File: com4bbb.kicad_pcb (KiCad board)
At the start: 2 copper layers, 54.6 x 86.4 mm, 50 parts, among them J101 PWR, J102 RS485, P8 BeagleBone_Black_Header, P9 BeagleBone_Black_Header, SW101 Reset, SW102 PWR, U101 WPMDH1100xx1S, U102 AT24C512C-SSHD-T, U103 SP3485EN, U104 ESP32-WROOM-32U

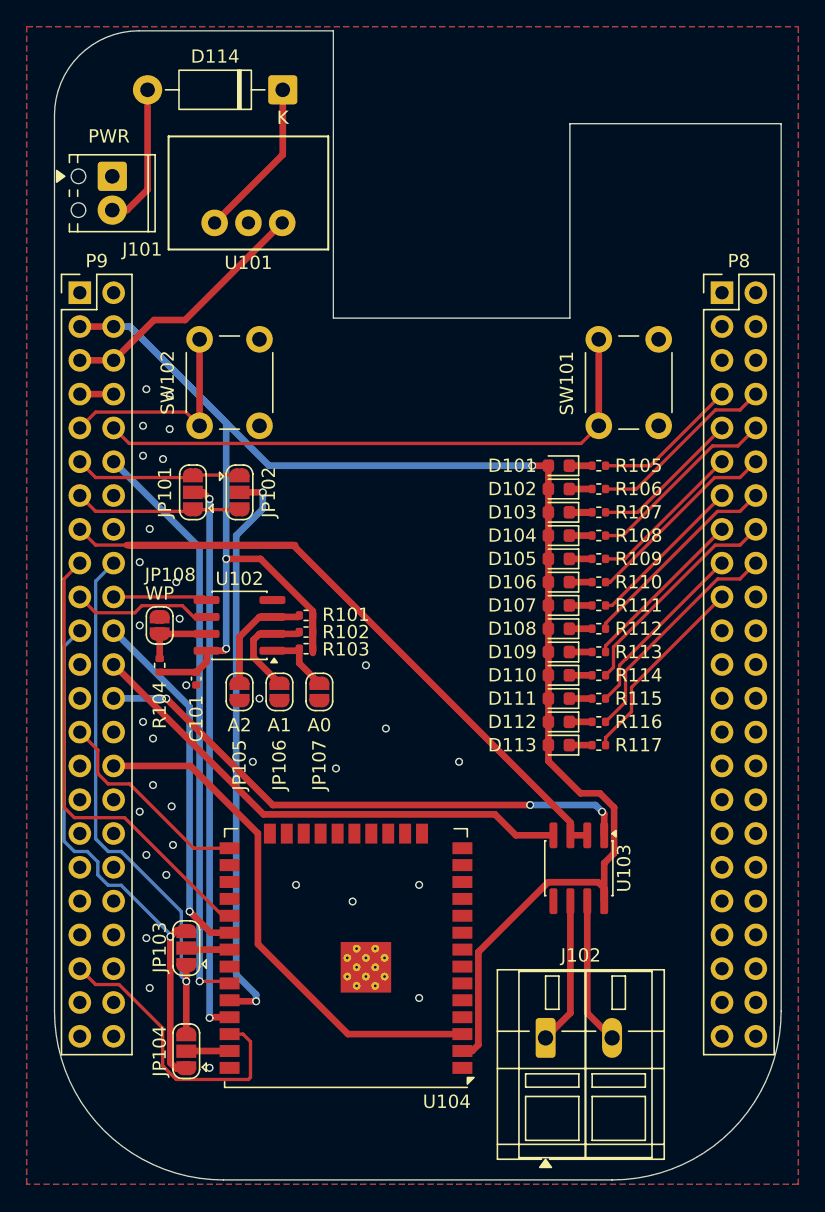
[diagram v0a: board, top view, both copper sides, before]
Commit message: Update to ESP32-S3-WROOM-1U
Signed-off-by: Benedikt Spranger <bene@eurovibes.org>
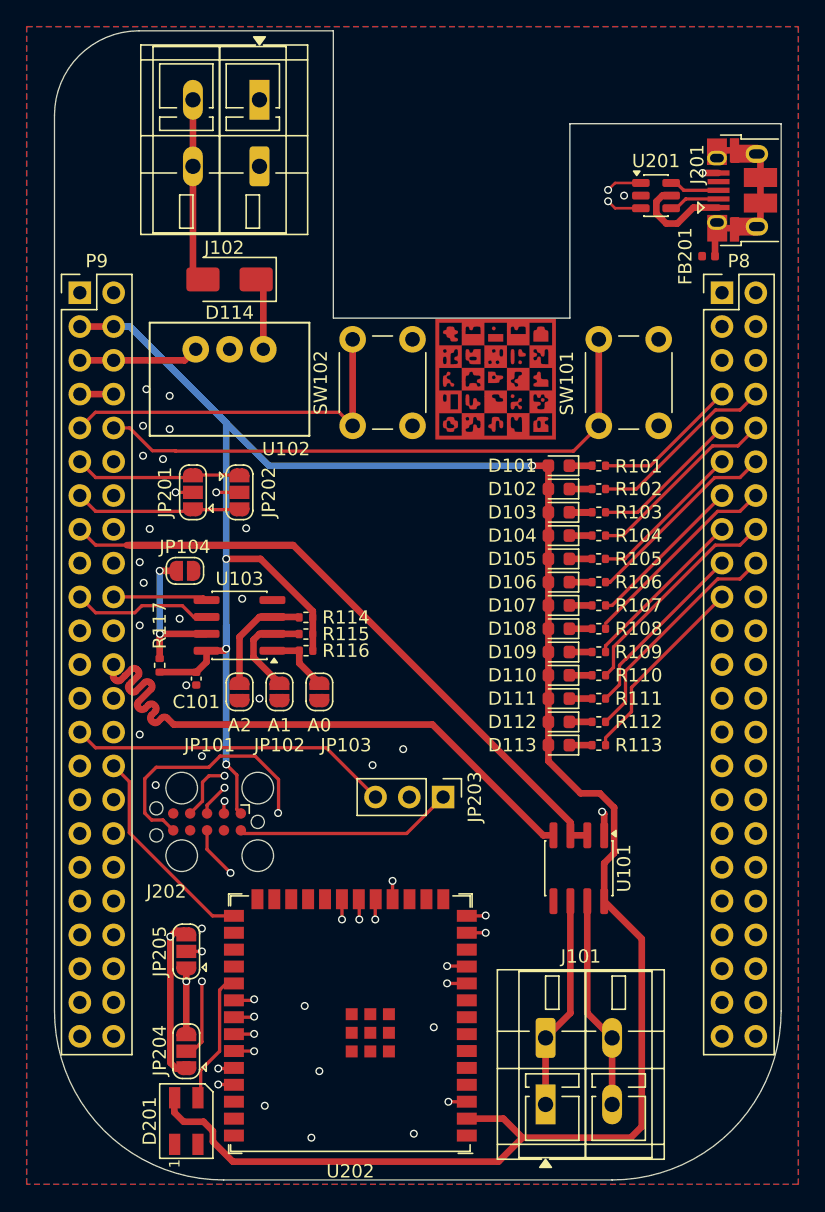
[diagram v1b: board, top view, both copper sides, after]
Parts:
- removed JP108: WP, Jumper:SolderJumper-2_P1.3mm_Open_RoundedPad1.0x1.5mm
- removed U104: ESP32-WROOM-32U, RF_Module:ESP32-WROOM-32U
- added D201: SK6812MINI, LED_SMD:LED_SK6812MINI_PLCC4_3.5x3.5mm_P1.75mm, F.Cu at (124.4, 124.6)
- added FB201: FerriteBead_Small, Inductor_SMD:L_0402_1005Metric, F.Cu at (163.6, 59.6)
- added G***: LOGO, eurovibes:LOGO, F.Cu at (147.6, 68.9)
- added J201: USB_B_Micro, Connector_USB:USB_Micro-B_Amphenol_10103594-0001LF_Horizontal, F.Cu at (166.1, 54.7)
- added J202: JTAG, Connector:Tag-Connect_TC2050-IDC-FP_2x05_P1.27mm_Vertical, F.Cu at (125.9, 102.1)
- added JP104: WP, Jumper:SolderJumper-2_P1.3mm_Open_RoundedPad1.0x1.5mm, F.Cu at (124.3, 83.3)
- added JP203: JTAG, Connector_PinHeader_2.54mm:PinHeader_1x03_P2.54mm_Vertical, F.Cu at (143.7, 100.3)
- added U201: USBLC6-2SC6, Package_TO_SOT_SMD:SOT-23-6, F.Cu at (159.7, 55.1)
- added U202: ESP32-S3-WROOM-1, PCM_Espressif:ESP32-S3-WROOM-1U, F.Cu at (136.7, 117.5)
- D114: value 1N4004 -> MRA4004T3G; footprint Diode_THT:D_DO-41_SOD81_P10.16mm_Horizontal -> Diode_SMD:D_SMA
- J101: renamed from J102; footprint TerminalBlock_WAGO:TerminalBlock_WAGO_236-102_1x02_P5.00mm_45Degree -> TerminalBlock_WAGO:TerminalBlock_WAGO_236-402_1x02_P5.00mm_45Degree
- J102: renamed from J101; footprint TerminalBlock_Phoenix:TerminalBlock_Phoenix_MPT-0,5-2-2.54_1x02_P2.54mm_Horizontal -> TerminalBlock_WAGO:TerminalBlock_WAGO_236-402_1x02_P5.00mm_45Degree
- moved R104 34.4 mm to (155.4, 80.6), turned to 0 degrees
- moved R117 33.5 mm to (122.4, 90.4), turned to 90 degrees
- moved R101 24.7 mm to (155.4, 75.4), turned to 0 degrees
- moved R102 24.5 mm to (155.4, 77.1), turned to 0 degrees
- moved R103 24.3 mm to (155.4, 78.9), turned to 0 degrees
- moved R116 22.6 mm to (133.4, 89.3), turned to 180 degrees
- moved R115 22.5 mm to (133.4, 88.0), turned to 180 degrees
- moved R114 22.4 mm to (133.4, 86.8), turned to 180 degrees
- moved D114 14.8 mm to (127.6, 61.4)
- moved SW102 11.5 mm to (136.9, 72.4)
- moved J102 11.1 mm to (129.9, 52.9), turned to 180 degrees
- moved U102 9.61 mm to (127.6, 66.6), turned to 180 degrees
- moved JP204 7.75 mm to (124.4, 119.4)
- moved JP205 7.50 mm to (124.4, 111.9)
- moved R105 7.00 mm to (155.4, 82.4)
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- renumbered JP105 to JP101, JP106 to JP102, JP107 to JP103, JP101 to JP201, JP102 to JP202, JP103 to JP204, JP104 to JP205, U103 to U101, U101 to U102, U102 to U103
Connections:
- JP101 pad 1: Net-(JP105-A) -> Net-(JP101-A)
- JP102 pad 1: Net-(JP106-A) -> Net-(JP102-A)
- JP103 pad 1: Net-(JP107-A) -> Net-(JP103-A)
- JP204 pad 1: /SPI0_D1 -> /SPI0_D0
- JP204 pad 3: /SPI0_D0 -> /SPI0_D1
- JP205 pad 1: /SPI0_D0 -> /SPI0_D1
- JP205 pad 3: /SPI0_D1 -> /SPI0_D0
- R101 pad 1: +3V3 -> Net-(D101-K)
- R101 pad 2: Net-(JP105-A) -> /LED0
- R102 pad 1: +3V3 -> Net-(D102-K)
- R102 pad 2: Net-(JP106-A) -> /LED1
- R103 pad 1: +3V3 -> Net-(D103-K)
- R103 pad 2: Net-(JP107-A) -> /LED2
- R104 pad 1: +3V3 -> Net-(D104-K)
- R104 pad 2: Net-(JP108-A) -> /LED3
- R105 pad 1: Net-(D101-K) -> Net-(D105-K)
- R105 pad 2: /LED0 -> /LED4
- R106 pad 1: Net-(D102-K) -> Net-(D106-K)
- R106 pad 2: /LED1 -> /LED5
- R107 pad 1: Net-(D103-K) -> Net-(D107-K)
- R107 pad 2: /LED2 -> /LED6
- R108 pad 1: Net-(D104-K) -> Net-(D108-K)
- R108 pad 2: /LED3 -> /LED7
- R109 pad 1: Net-(D105-K) -> Net-(D109-K)
- R109 pad 2: /LED4 -> /LED8
- R110 pad 1: Net-(D106-K) -> Net-(D110-K)
- R110 pad 2: /LED5 -> /LED9
- R111 pad 1: Net-(D107-K) -> Net-(D111-K)
- R111 pad 2: /LED6 -> /LED10
- R112 pad 1: Net-(D108-K) -> Net-(D112-K)
- R112 pad 2: /LED7 -> /LED11
- R113 pad 1: Net-(D109-K) -> Net-(D113-K)
- R113 pad 2: /LED8 -> /LED12
- R114 pad 1: Net-(D110-K) -> +3V3
- R114 pad 2: /LED9 -> Net-(JP101-A)
- R115 pad 1: Net-(D111-K) -> +3V3
- R115 pad 2: /LED10 -> Net-(JP102-A)
- R116 pad 1: Net-(D112-K) -> +3V3
- R116 pad 2: /LED11 -> Net-(JP103-A)
- R117 pad 1: Net-(D113-K) -> +3V3
- R117 pad 2: /LED12 -> Net-(JP104-A)
- U103 pad 1: Net-(JP107-A) -> Net-(JP103-A)
- U103 pad 2: Net-(JP106-A) -> Net-(JP102-A)
- U103 pad 3: Net-(JP105-A) -> Net-(JP101-A)
- U103 pad 7: Net-(JP108-A) -> Net-(JP104-A)
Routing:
- net /ESP32/D-: track 0.00 -> 64.1 mm, vias 0 -> 2
- net /ESP32/D+: track 0.00 -> 64.1 mm, vias 0 -> 2
- net +3V3: track 144.1 -> 205.6 mm, vias 3 -> 4
- net /ESP32/TDO: track 0.00 -> 36.9 mm, vias 0 -> 2
- net Net-(JP203-C): track 0.00 -> 25.6 mm, vias 0 -> 1
- net /ESP32/TCK: track 0.00 -> 23.9 mm, vias 0 -> 2
- net /ESP32/TMS: track 0.00 -> 23.5 mm, vias 0 -> 2
- net /GPIO_122: track 39.2 -> 16.0 mm
- net Net-(JP204-C): track 3.38 -> 22.5 mm, vias 0 -> 2
- net /ESP32/TDI: track 0.00 -> 18.3 mm, vias 0 -> 2
- net /ESP32/~{RST}: track 0.00 -> 16.4 mm
- net /SPI0_SCLK: track 27.4 -> 39.3 mm, vias 1 -> 2
- net PWR_BUT: track 16.4 -> 27.9 mm
- net Net-(JP104-A): track 0.00 -> 11.3 mm, vias 0 -> 2
- net Net-(JP205-C): track 3.48 -> 14.2 mm, vias 0 -> 2
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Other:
- copper layers 2 -> 4

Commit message: Add RTC and secure memory
Signed-off-by: Benedikt Spranger <bene@eurovibes.org>
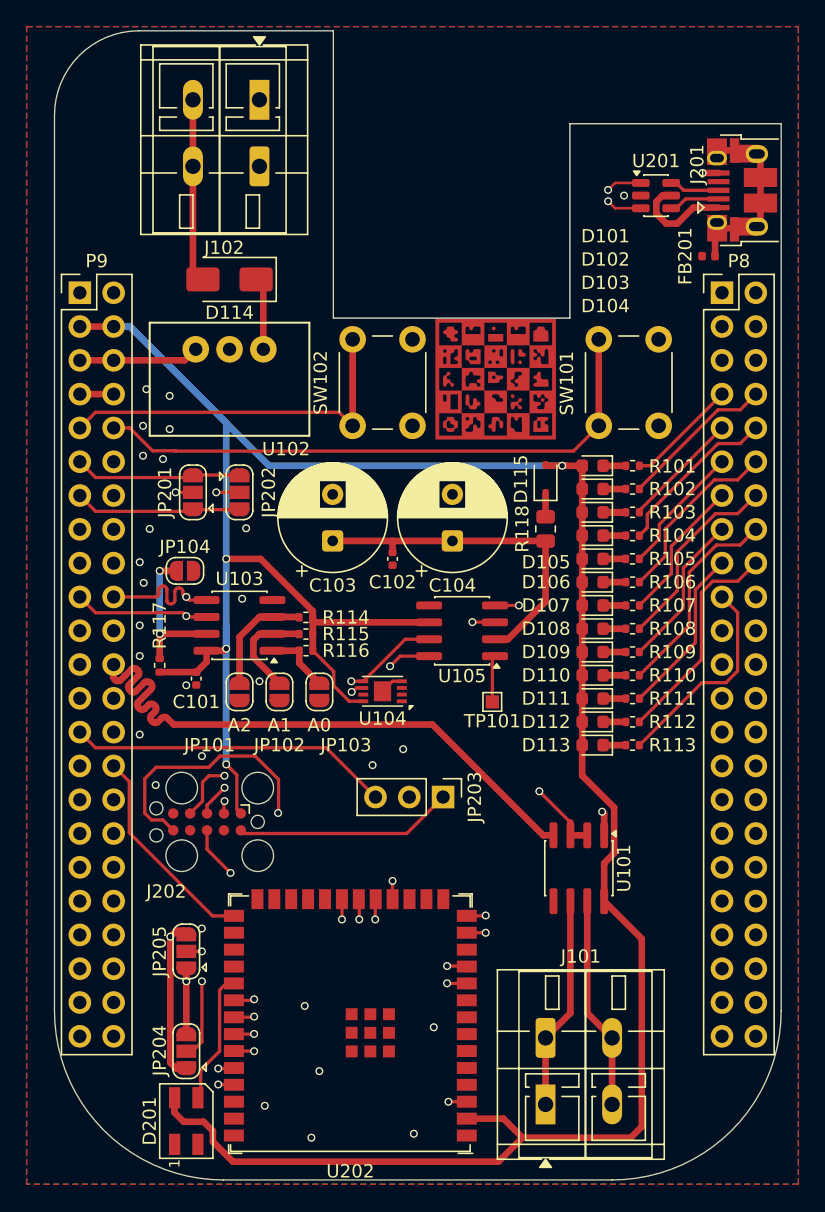
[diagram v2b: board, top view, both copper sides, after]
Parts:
- added C102: 100n, Capacitor_SMD:C_0402_1005Metric, F.Cu at (139.9, 82.4)
- added C103: 1F, Capacitor_THT:CP_Radial_D8.0mm_P3.50mm, F.Cu at (135.4, 81.0)
- added C104: 1F, Capacitor_THT:CP_Radial_D8.0mm_P3.50mm, F.Cu at (144.4, 81.0)
- added D115: 1N5819WS, Diode_SMD:D_SOD-323, F.Cu at (151.4, 76.4)
- added R118: 15, Resistor_SMD:R_0805_2012Metric, F.Cu at (151.4, 80.1)
- added TP101: 32kHz, TestPoint:TestPoint_Pad_1.0x1.0mm, F.Cu at (147.4, 93.1)
- added U104: ATECC608A-MAHDA, Package_DFN_QFN:DFN-8-1EP_3x2mm_P0.5mm_EP1.3x1.5mm, F.Cu at (139.1, 92.3)
- added U105: DS3231MZ, Package_SO:SOIC-8_3.9x4.9mm_P1.27mm, F.Cu at (145.1, 87.8)
- U102: value WPMDH1100xx1S -> R-78K5.0-0.5
- moved R105 2.54 mm to (157.9, 82.4)
- moved D101 2.54 mm to (154.9, 75.4)
- moved D102 2.54 mm to (154.9, 77.1)
- moved D103 2.54 mm to (154.9, 78.9)
- moved D104 2.54 mm to (154.9, 80.6)
- moved D105 2.54 mm to (154.9, 82.4)
- moved D106 2.54 mm to (154.9, 84.1)
- moved D107 2.54 mm to (154.9, 85.9)
- moved D108 2.54 mm to (154.9, 87.6)
- moved D109 2.54 mm to (154.9, 89.4)
- moved D110 2.54 mm to (154.9, 91.1)
- moved D111 2.54 mm to (154.9, 92.9)
- moved D112 2.54 mm to (154.9, 94.6)
- moved D113 2.54 mm to (154.9, 96.4)
- moved R101 2.54 mm to (157.9, 75.4)
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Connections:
- P9 pad 14: unconnected-(P9-Pin_14-Pad14) -> /RTC_INT
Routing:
- net /RTC_INT: track 0.00 -> 32.6 mm, vias 0 -> 1
- net /Vbat: track 0.00 -> 26.4 mm
- net /SDA: track 7.08 -> 32.3 mm, vias 0 -> 2
- net /SCL: track 10.6 -> 33.1 mm, vias 0 -> 3
- net SYS_RESETN: track 44.5 -> 62.3 mm, vias 0 -> 1
- net +3V3: track 205.6 -> 222.5 mm
- net /GPIO_48: track 60.7 -> 49.2 mm, vias 0 -> 1
- net Net-(U105-32KHZ): track 0.00 -> 3.52 mm
- net /LED0: track 11.0 -> 8.44 mm
- net /LED1: track 14.2 -> 11.7 mm
- net /LED2: track 11.4 -> 8.91 mm
- net /LED3: track 14.6 -> 12.7 mm
- net /LED4: track 11.8 -> 9.88 mm
- net Net-(D115-K): track 0.00 -> 1.79 mm
- net GNDD: track 3.68 -> 5.44 mm
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
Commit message: Change jumper position
Signed-off-by: Benedikt Spranger <bene@eurovibes.org>
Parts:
- moved JP203 7.85 mm to (135.8, 99.9), turned to 90 degrees
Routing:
- net /ESP32/~{RST}: track 16.4 -> 8.76 mm
- net /GPIO_125: track 24.2 -> 26.4 mm
- net Net-(JP203-C): track 25.6 -> 27.0 mm
- net GNDD: vias 28 -> 31
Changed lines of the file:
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@@
 	(footprint "Connector_PinHeader_2.54mm:PinHeader_1x03_P2.54mm_Vertical"
 		(layer "F.Cu")
-		(at 143.6701 100.2824 -90)
+		(at 135.8301 99.8824 90)
 		(descr "Through hole straight pin header, 1x03, 2.54mm pitch, single row")
 		(tags "Through hole pin header THT 1x03 2.54mm single row")
@@
 		)
 		(property "Long Description" "Connector: pin strips; pin header; male; PIN: 3; THT; straight; 1x3"
-			(at 0 0 270)
+			(at 0 0 90)
 			(unlocked yes)
 			(layer "F.Fab")
@@
 		)
 		(property "Source" "TME"
-			(at 0 0 270)
+			(at 0 0 90)
 			(unlocked yes)
 			(layer "F.Fab")
@@
 		)
 		(property "SupplLink" "https://www.tme.eu/de/en/details/zl201-03g/pin-headers/connfly/ds1021-1-3sf11-b/"
-			(at 0 0 270)
+			(at 0 0 90)
 			(unlocked yes)
 			(layer "F.Fab")
@@
 		)
 		(property "digikey#" ""
-			(at 0 0 270)
+			(at 0 0 90)
 			(unlocked yes)
 			(layer "F.Fab")
@@
 		)
 		(property "tme#" "ZL201-03G"
-			(at 0 0 270)
+			(at 0 0 90)
 			(unlocked yes)
 			(layer "F.Fab")
@@
 		)
 		(property "assemble" "n"
-			(at 0 0 270)
+			(at 0 0 90)
 			(unlocked yes)
 			(layer "F.Fab")
@@
 		)
 		(property "MF" "CONNFLY"
-			(at 0 0 270)
+			(at 0 0 90)
 			(unlocked yes)
 			(layer "F.Fab")
@@
 		)
 		(property "MP" "DS1021-1*3SF11-B"
-			(at 0 0 270)
+			(at 0 0 90)
 			(unlocked yes)
 			(layer "F.Fab")
@@
 		(attr through_hole exclude_from_bom)
 		(fp_line
-			(start -1.38 6.46)
-			(end 1.38 6.46)
+			(start -1.38 -1.38)
+			(end 0 -1.38)
 			(stroke
 				(width 0.12)
@@
 		)
 		(fp_line
-			(start -1.38 1.27)
-			(end -1.38 6.46)
+			(start -1.38 0)
+			(end -1.38 -1.38)
 			(stroke
 				(width 0.12)
@@
 		)
 		(fp_line
-			(start -1.38 1.27)
-			(end 1.38 1.27)
+			(start 1.38 1.27)
+			(end 1.38 6.46)
 			(stroke
 				(width 0.12)
@@
 		)
 		(fp_line
-			(start 1.38 1.27)
-			(end 1.38 6.46)
+			(start -1.38 1.27)
+			(end 1.38 1.27)
 			(stroke
 				(width 0.12)
@@
 		)
 		(fp_line
-			(start -1.38 0)
-			(end -1.38 -1.38)
+			(start -1.38 1.27)
+			(end -1.38 6.46)
 			(stroke
 				(width 0.12)
@@
 		)
 		(fp_line
-			(start -1.38 -1.38)
-			(end 0 -1.38)
+			(start -1.38 6.46)
+			(end 1.38 6.46)
 			(stroke
 				(width 0.12)
@@
 		)
 		(fp_line
-			(start -1.77 6.85)
-			(end 1.77 6.85)
+			(start 1.77 -1.77)
+			(end -1.77 -1.77)
 			(stroke
 				(width 0.05)
@@
 		)
 		(fp_line
-			(start 1.77 6.85)
-			(end 1.77 -1.77)
+			(start -1.77 -1.77)
+			(end -1.77 6.85)
 			(stroke
 				(width 0.05)
@@
 		)
 		(fp_line
-			(start -1.77 -1.77)
-			(end -1.77 6.85)
+			(start 1.77 6.85)
+			(end 1.77 -1.77)
 			(stroke
 				(width 0.05)
@@
 		)
 		(fp_line
-			(start 1.77 -1.77)
-			(end -1.77 -1.77)
+			(start -1.77 6.85)
+			(end 1.77 6.85)
 			(stroke
 				(width 0.05)
@@
 		)
 		(fp_line
-			(start -1.27 6.35)
-			(end -1.27 -0.635)
+			(start 1.27 -1.27)
+			(end 1.27 6.35)
 			(stroke
 				(width 0.1)
@@
 		)
 		(fp_line
-			(start 1.27 6.35)
-			(end -1.27 6.35)
+			(start -0.635 -1.27)
+			(end 1.27 -1.27)
 			(stroke
 				(width 0.1)
@@
 		)
 		(fp_line
-			(start -0.635 -1.27)
-			(end 1.27 -1.27)
+			(start 1.27 6.35)
+			(end -1.27 6.35)
 			(stroke
 				(width 0.1)
@@
 		)
 		(fp_line
-			(start 1.27 -1.27)
-			(end 1.27 6.35)
+			(start -1.27 6.35)
+			(end -1.27 -0.635)
 			(stroke
 				(width 0.1)
@@
 		)
 		(pad "1" thru_hole rect
-			(at 0 0 270)
+			(at 0 0 90)
 			(size 1.7 1.7)
 			(drill 1)
@@
 		)
 		(pad "2" thru_hole circle
-			(at 0 2.54 270)
+			(at 0 2.54 90)
 			(size 1.7 1.7)
 			(drill 1)
@@
 		)
 		(pad "3" thru_hole circle
-			(at 0 5.08 270)
+			(at 0 5.08 90)
 			(size 1.7 1.7)
 			(drill 1)
@@
 	)
 	(via
+		(at 148.1201 107.8824)
+		(size 0.6)
+		(drill 0.4)
+		(layers "F.Cu" "B.Cu")
+		(free yes)
+		(net 1)
+	)
+	(via
 		(at 120.8701 95.5824)
 		(size 0.6)
@@
 	)
 	(via
+		(at 144.1201 101.1324)
+		(size 0.6)
+		(drill 0.4)
+		(layers "F.Cu" "B.Cu")
+		(free yes)
+		(net 1)
+	)
+	(via
 		(at 120.8701 82.6324)
 		(size 0.6)
@@
 	)
 	(via
+		(at 135.8701 104.8824)
+		(size 0.6)
+		(drill 0.4)
+		(layers "F.Cu" "B.Cu")
+		(free yes)
+		(net 1)
+	)
+	(via
 		(at 121.1201 72.3824)
 		(size 0.6)
@@
 	)
 	(via
-		(at 140.6701 96.6824)
+		(at 132.3701 97.6324)
 		(size 0.6)
 		(drill 0.4)
@@
 	)
 	(via
-		(at 138.3701 97.8824)
+		(at 137.3701 97.3824)
 		(size 0.6)
 		(drill 0.4)
@@
 	)
 	(segment
-		(start 143.6701 100.2824)
-		(end 140.9328 103.0197)
+		(start 132.6928 103.0197)
+		(end 135.8301 99.8824)
 		(width 0.25)
 		(layer "F.Cu")
@@
 	)
 	(segment
-		(start 128.7064 103.0197)
-		(end 128.4701 102.7834)
+		(start 128.4701 102.7834)
+		(end 128.7064 103.0197)
 		(width 0.25)
 		(layer "F.Cu")
@@
 	)
 	(segment
-		(start 140.9328 103.0197)
-		(end 128.7064 103.0197)
+		(start 128.7064 103.0197)
+		(end 132.6928 103.0197)
 		(width 0.25)
 		(layer "F.Cu")
@@
 	)
 	(segment
-		(start 116.3701 95.4024)
-		(end 117.5461 96.5784)
+		(start 117.5461 96.5784)
+		(end 137.6061 96.5784)
 		(width 0.25)
 		(layer "F.Cu")
@@
 	)
 	(segment
-		(start 134.8861 96.5784)
-		(end 138.5901 100.2824)
+		(start 137.6061 96.5784)
+		(end 140.9101 99.8824)
 		(width 0.25)
 		(layer "F.Cu")
@@
 	)
 	(segment
-		(start 117.5461 96.5784)
-		(end 134.8861 96.5784)
+		(start 116.3701 95.4024)
+		(end 117.5461 96.5784)
 		(width 0.25)
 		(layer "F.Cu")
@@
 	)
 	(segment
-		(start 141.1301 120.4424)
-		(end 143.8701 123.1824)
+		(start 144.0701 123.1824)
+		(end 139.2201 118.3324)
 		(width 0.25)
 		(layer "In2.Cu")
@@
 	)
 	(segment
-		(start 143.8701 123.1824)
-		(end 144.0701 123.1824)
+		(start 139.2201 100.7324)
+		(end 138.3701 99.8824)
 		(width 0.25)
 		(layer "In2.Cu")
@@
 	)
 	(segment
-		(start 141.1301 100.2824)
-		(end 141.1301 120.4424)
+		(start 139.2201 118.3324)
+		(end 139.2201 100.7324)
 		(width 0.25)
 		(layer "In2.Cu")

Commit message: Add DCF77 clock input
Signed-off-by: Benedikt Spranger <b.spranger@linutronix.de>
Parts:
- added J103: DCF77, Connector_PinHeader_2.54mm:PinHeader_1x02_P2.54mm_Vertical, F.Cu at (117.6, 54.6)
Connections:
- P9 pad 16: unconnected-(P9-Pin_16-Pad16) -> /DCF77
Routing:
- net /DCF77: track 0.00 -> 27.0 mm
